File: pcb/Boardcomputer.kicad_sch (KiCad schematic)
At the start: 17 parts, among them J1 Receiver, J2 5V Input, J3 5V Reg VCC, M1 Winch Rear, M2 Motor, M3 Winch Front, M4 Steering Servo, Q1 Motor VCC, U1 ESP32 C3 SUPERMINI, U2 Winch Rear VCC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

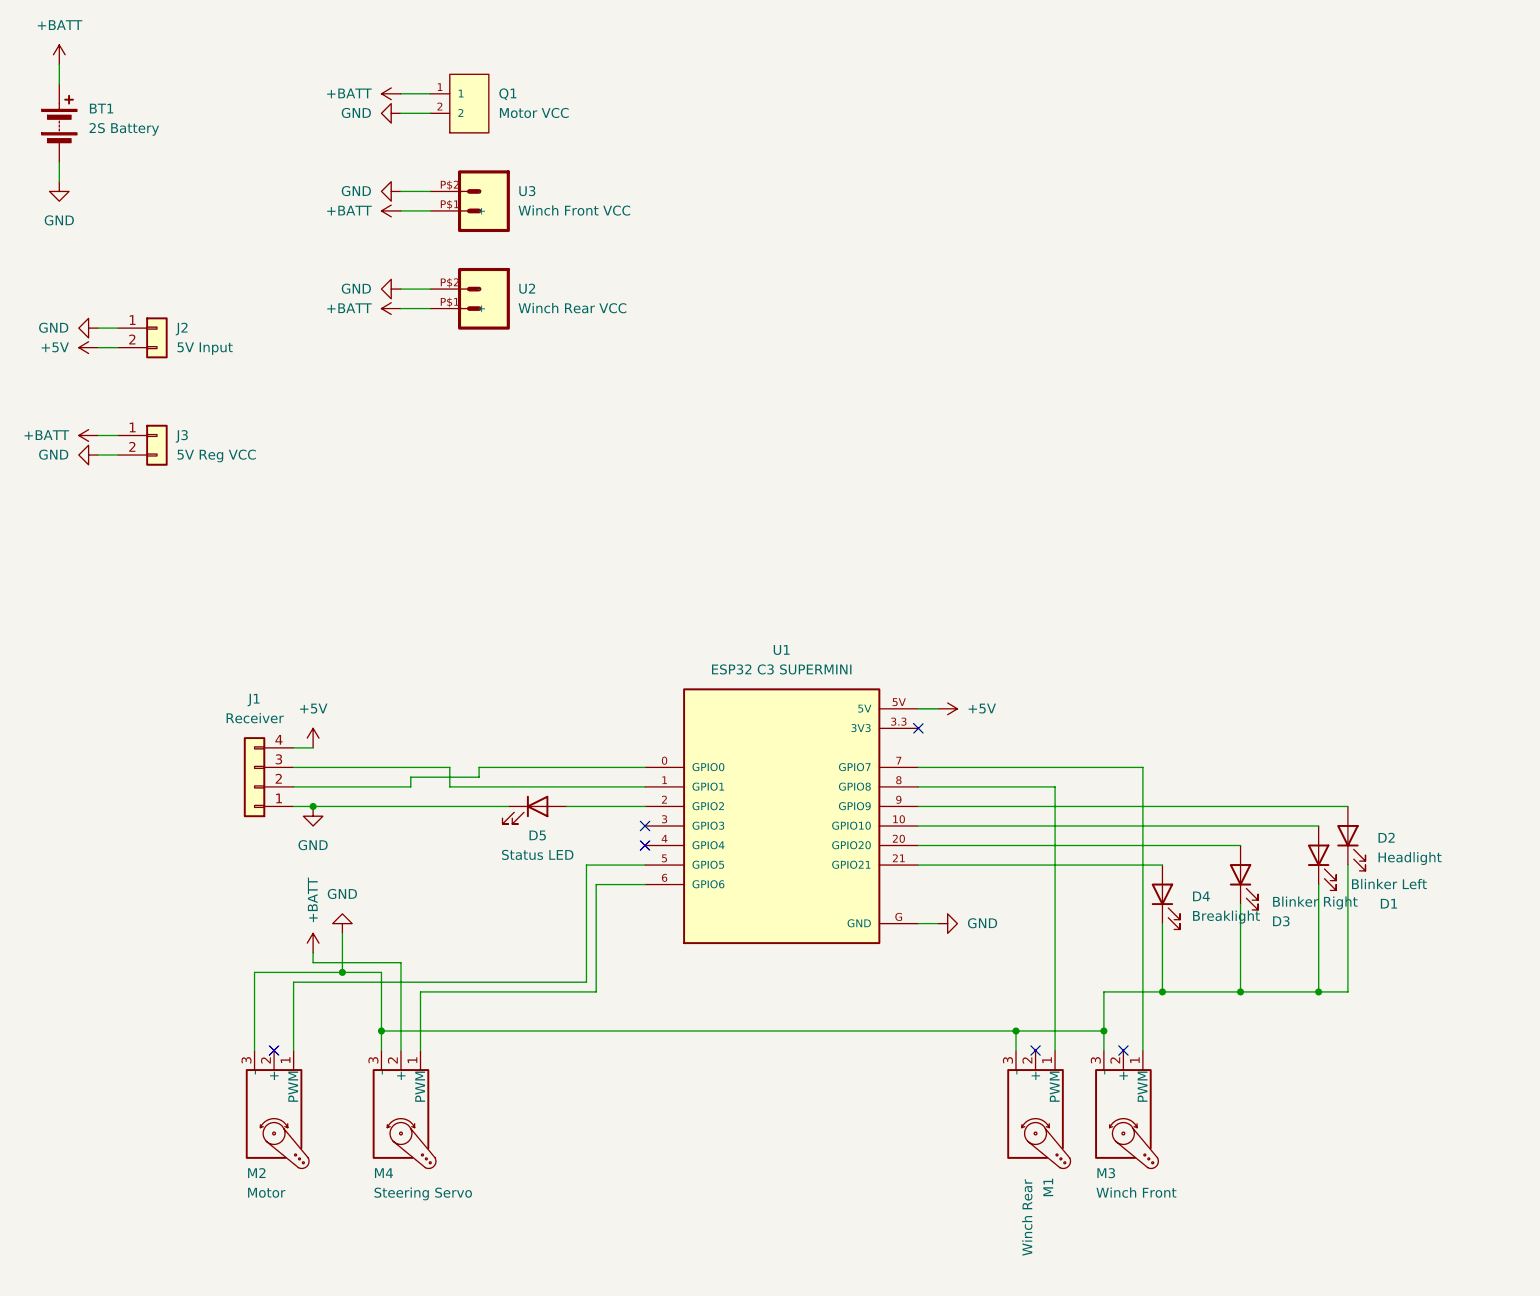
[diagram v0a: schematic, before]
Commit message: Way too much stuff for one commit... essentially made everything configurable through a web ui
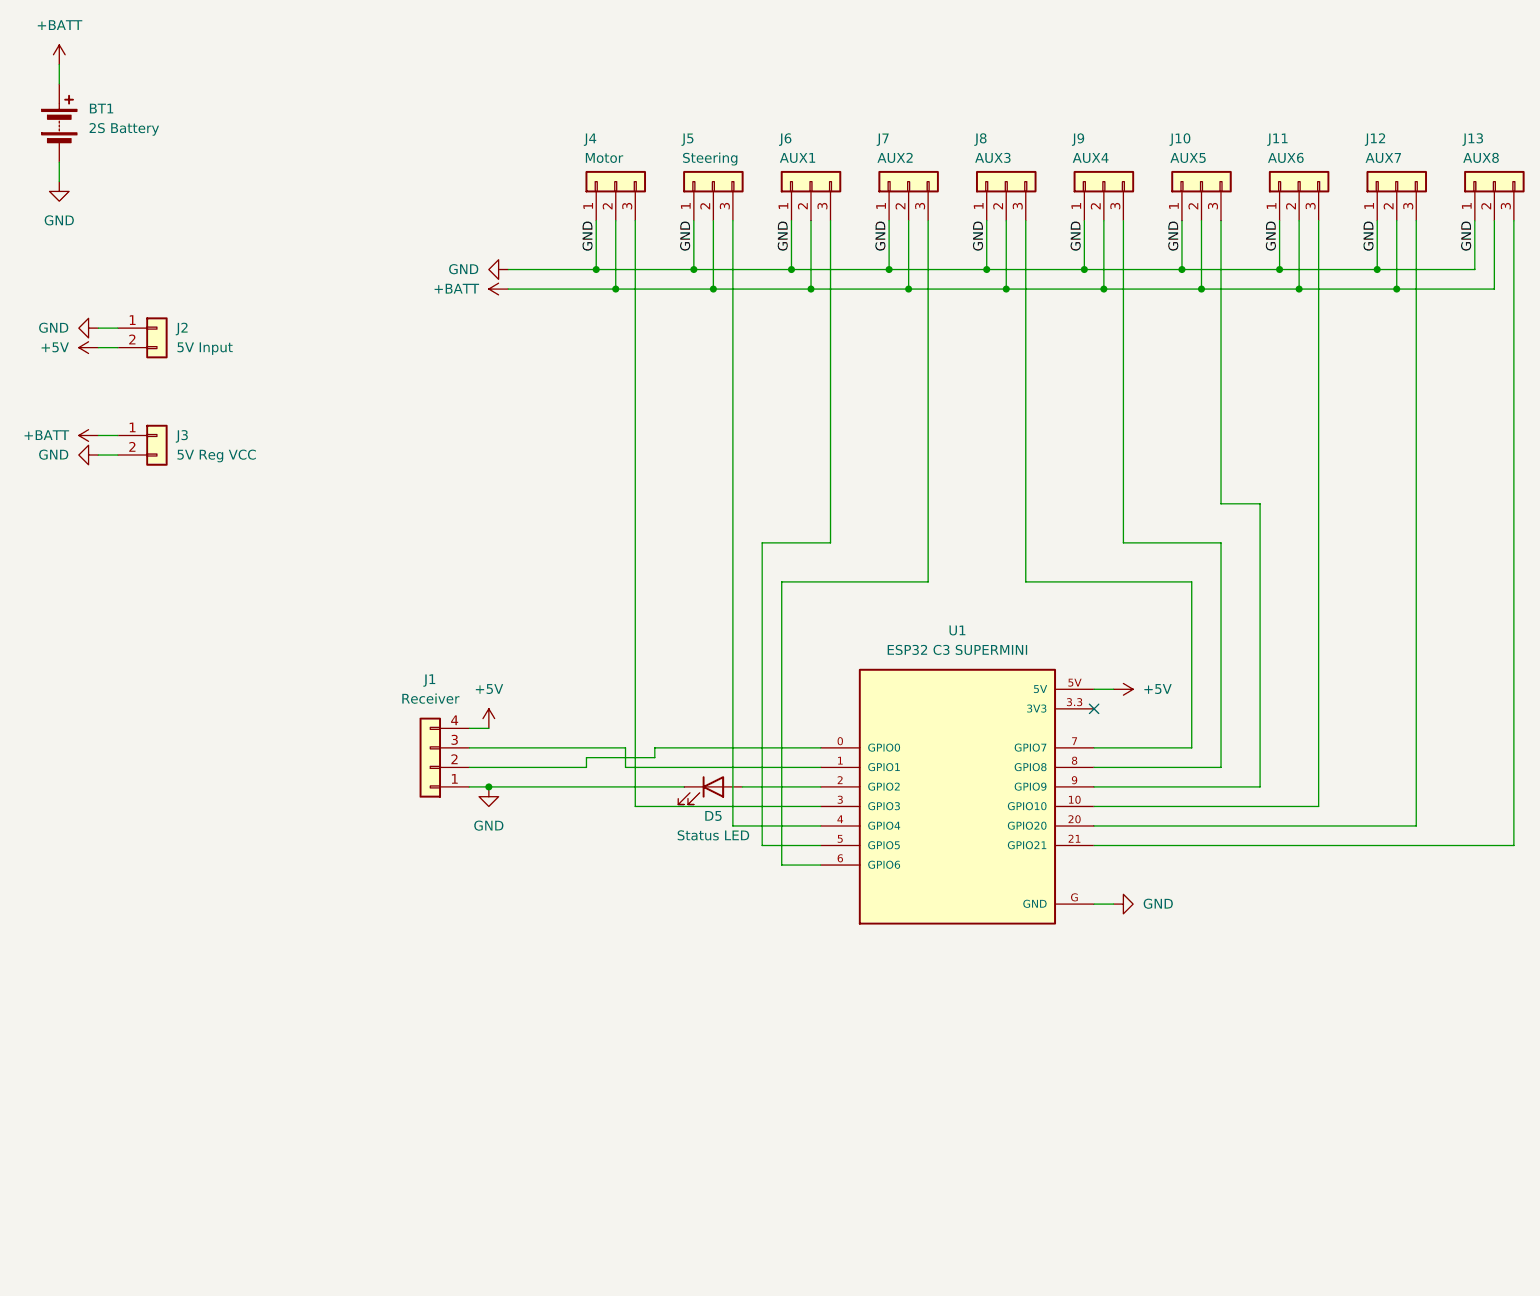
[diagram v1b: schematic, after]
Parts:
- removed D1: Blinker Left, Connector_PinHeader_2.54mm:PinHeader_2x01_P2.54mm_Vertical, symbol Device:LED
- removed D2: Headlight, Connector_PinHeader_2.54mm:PinHeader_2x01_P2.54mm_Vertical, symbol Device:LED
- removed D3: Blinker Right, Connector_PinHeader_2.54mm:PinHeader_2x01_P2.54mm_Vertical, symbol Device:LED
- removed D4: Breaklight, Connector_PinHeader_2.54mm:PinHeader_2x01_P2.54mm_Vertical, symbol Device:LED
- removed M1: Winch Rear, Connector_PinHeader_2.54mm:PinHeader_1x03_P2.54mm_Vertical, symbol Motor:Motor_Servo
- removed M2: Motor, Connector_PinHeader_2.54mm:PinHeader_1x03_P2.54mm_Vertical, symbol Motor:Motor_Servo
- removed M3: Winch Front, Connector_PinHeader_2.54mm:PinHeader_1x03_P2.54mm_Vertical, symbol Motor:Motor_Servo
- removed M4: Steering Servo, Connector_PinHeader_2.54mm:PinHeader_1x03_P2.54mm_Vertical, symbol Motor:Motor_Servo
- removed Q1: Motor VCC, Library:AMASS_XT60PB-M, symbol XT60_YELLOW:XT60_YELLOW
- removed U2: Winch Rear VCC, Library:XT30UPB-M, symbol XT30UPB-M:XT30UPB-M
- removed U3: Winch Front VCC, Library:XT30UPB-M, symbol XT30UPB-M:XT30UPB-M
- added J10: AUX5, Connector_PinHeader_2.54mm:PinHeader_1x03_P2.54mm_Vertical, symbol Connector_Generic:Conn_01x03
- added J11: AUX6, Connector_PinHeader_2.54mm:PinHeader_1x03_P2.54mm_Vertical, symbol Connector_Generic:Conn_01x03
- added J12: AUX7, Connector_PinHeader_2.54mm:PinHeader_1x03_P2.54mm_Vertical, symbol Connector_Generic:Conn_01x03
- added J13: AUX8, Connector_PinHeader_2.54mm:PinHeader_1x03_P2.54mm_Vertical, symbol Connector_Generic:Conn_01x03
- added J4: Motor, Connector_PinHeader_2.54mm:PinHeader_1x03_P2.54mm_Vertical, symbol Connector_Generic:Conn_01x03
- added J5: Steering, Connector_PinHeader_2.54mm:PinHeader_1x03_P2.54mm_Vertical, symbol Connector_Generic:Conn_01x03
- added J6: AUX1, Connector_PinHeader_2.54mm:PinHeader_1x03_P2.54mm_Vertical, symbol Connector_Generic:Conn_01x03
- added J7: AUX2, Connector_PinHeader_2.54mm:PinHeader_1x03_P2.54mm_Vertical, symbol Connector_Generic:Conn_01x03
- added J8: AUX3, Connector_PinHeader_2.54mm:PinHeader_1x03_P2.54mm_Vertical, symbol Connector_Generic:Conn_01x03
- added J9: AUX4, Connector_PinHeader_2.54mm:PinHeader_1x03_P2.54mm_Vertical, symbol Connector_Generic:Conn_01x03
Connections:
- net +BATT: now also J10.2 (Pin_2), J11.2 (Pin_2), J12.2 (Pin_2), J13.2 (Pin_2), J4.2 (Pin_2), J5.2 (Pin_2), J6.2 (Pin_2), J7.2 (Pin_2), J8.2 (Pin_2), J9.2 (Pin_2)
- net GND: now also J10.1 (Pin_1), J11.1 (Pin_1), J12.1 (Pin_1), J13.1 (Pin_1), J4.1 (Pin_1), J5.1 (Pin_1), J6.1 (Pin_1), J7.1 (Pin_1), J8.1 (Pin_1), J9.1 (Pin_1)
- net at U1.10 (GPIO10): now also J11.3 (Pin_3)
- net at U1.5 (GPIO5): now also J6.3 (Pin_3)
- net at U1.9 (GPIO9): now also J10.3 (Pin_3)
- net at U1.7 (GPIO7): now also J8.3 (Pin_3)
- net at U1.20 (GPIO20): now also J12.3 (Pin_3)
- net at U1.21 (GPIO21): now also J13.3 (Pin_3)
- net at U1.3 (GPIO3): now also J4.3 (Pin_3)
- net at U1.4 (GPIO4): now also J5.3 (Pin_3)
- net at U1.6 (GPIO6): now also J7.3 (Pin_3)
- net at U1.8 (GPIO8): now also J9.3 (Pin_3)
- no-connect marks 6 -> 1
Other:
- moved on the sheet: D5, J1, U1
